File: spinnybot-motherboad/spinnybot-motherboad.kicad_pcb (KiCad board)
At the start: 2 copper layers, 109.4 x 86 mm, 78 parts, among them J1 ENCODER 1, J10 ESC_POS, J11 POWER SW2, J12 LEDSTRIP3, J13 LEDSTRIP2, J14 LEDSTRIP3, J15 BAT_GND, J16 ESC_GND, J2 LEDSTRIP1, J3 LEDSTRIP1, J4 LEDSTRIP2, J5 ENCODER 2, J6 ENCODER 3, J7 SM10B-SRSS-TB, J8 BAT_POS, J9 POWER SW1, Q1 SISA96DN, Q2 SISA96DN, Q3 BC846, Q4 Q_NMOS_DGS, U1 LM1117-3.3, U10 MMA3221KEG, U11 ADS122U04IPWR, U12 ADS122U04IPWR, U2 XBP9B-DMWTB002, U3 MC14504BDR2G, U4 ICM-20649, U5 ESP32-DEVKITC-32D, U6 74LVC1G157GV_125, U7 SN74AHCT541DW, U8 SN74LVC1G18DBVR, U9 MMA3221KEG

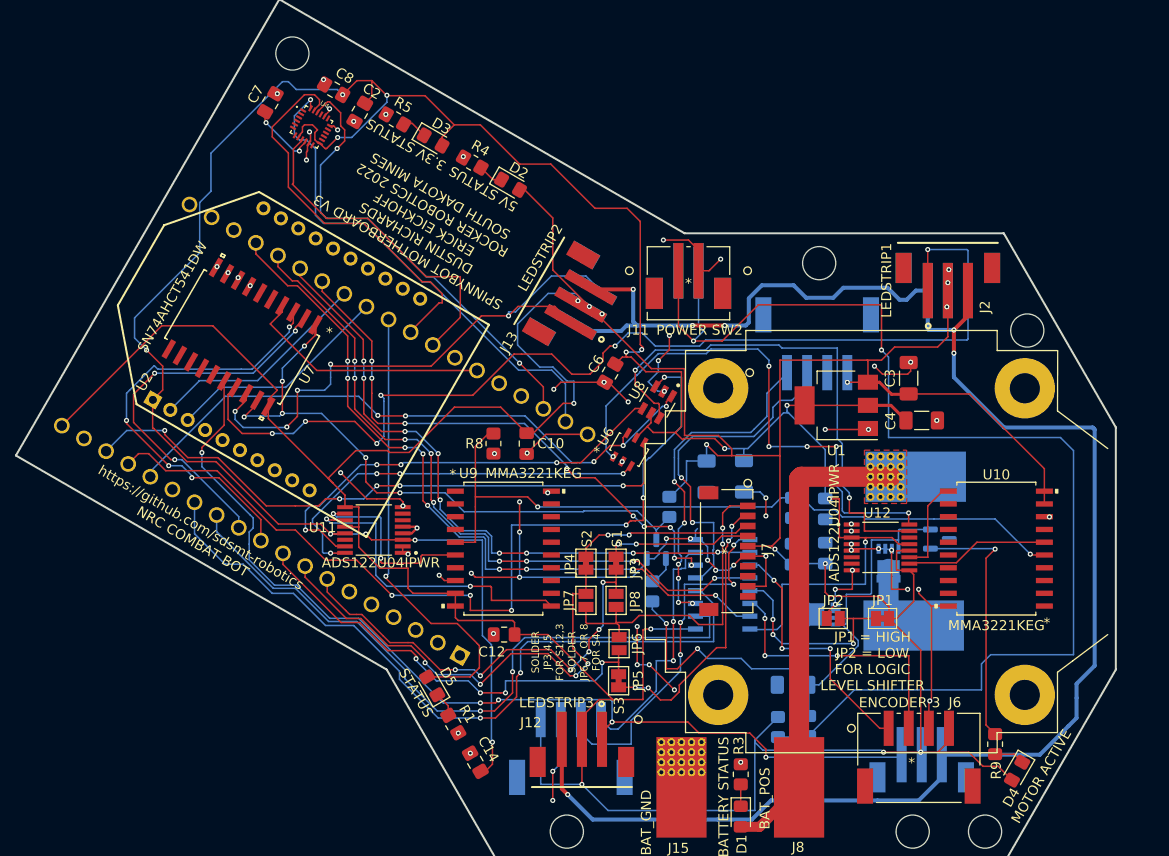
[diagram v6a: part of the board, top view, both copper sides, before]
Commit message: Addressed Pratik's concerns about cap placement and missing caps
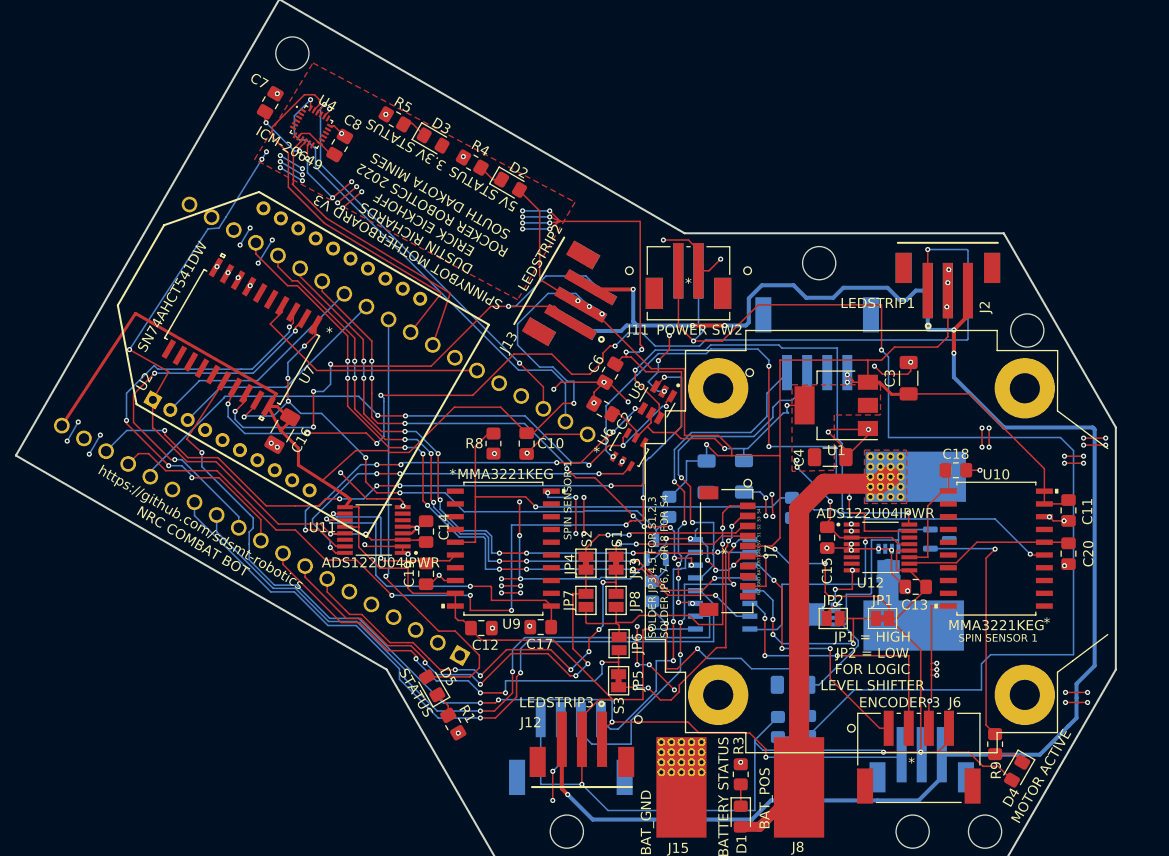
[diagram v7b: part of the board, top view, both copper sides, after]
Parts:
- added C16: 0.1u, Capacitor_SMD:C_1206_3216Metric_Pad1.33x1.80mm_HandSolder, F.Cu at (114.6, 107.1)
- added C17: 10nF, Capacitor_SMD:C_0805_2012Metric_Pad1.18x1.45mm_HandSolder, F.Cu at (140.3, 126.6)
- added C18: 10nF, Capacitor_SMD:C_0805_2012Metric_Pad1.18x1.45mm_HandSolder, F.Cu at (181.6, 111.0)
- added C19: 10nF, Capacitor_SMD:C_0805_2012Metric_Pad1.18x1.45mm_HandSolder, F.Cu at (128.9, 121.3)
- added C20: 10nF, Capacitor_SMD:C_0805_2012Metric_Pad1.18x1.45mm_HandSolder, F.Cu at (192.8, 119.3)
- C11, C13, C15: moved to F.Cu
- moved C2 38.2 mm to (146.5, 104.9), turned to 150 degrees
- moved C11 24.6 mm to (192.8, 115.0), turned to -90 degrees
- moved C14 23.5 mm to (128.9, 117.1), turned to 90 degrees
- moved C13 12.7 mm to (177.6, 122.6), turned to 180 degrees
- moved C4 9.81 mm to (169.1, 109.7)
- moved C8 5.59 mm to (120.3, 78.7), turned to 60 degrees
- moved C15 2.86 mm to (168.8, 117.7)
- moved C12 2.35 mm to (134.4, 126.7), turned to 0 degrees
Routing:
- net +3V3: track 272.1 -> 198.1 mm, vias 14 -> 27
- net GND: track 161.3 -> 235.1 mm, vias 70 -> 116
- net +5V: track 400.5 -> 410.3 mm, vias 15 -> 16
- net /IMU_CS: track 45.8 -> 40.7 mm
- net /MISO_3V3: track 33.3 -> 29.5 mm
- net /MOSI_3V3: track 49.9 -> 47.1 mm
- net Net-(U10-Pad6): track 14.3 -> 16.8 mm
- net Net-(U10-Pad11): track 9.59 -> 11.8 mm
- net Net-(U11-Pad11): track 31.6 -> 33.7 mm
- net +12V: track 47.1 -> 45.3 mm
- net /SCK_3V3: track 39.2 -> 37.7 mm
- net /LEDSTRIP1_DATA_5V: track 106.3 -> 105.1 mm
- net /MCU and Buffers/ENC_1B_3V3: track 74.6 -> 73.7 mm
- net /LEDSTRIP3_DATA_5V: track 98.2 -> 99.1 mm
- net /IMU and Accelerometers/ADC1_RX: track 39.8 -> 39.1 mm
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- added copper zone on F.Cu, net +3V3
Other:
- board text added: "N/C GND BAT CRT GND 5V S1 S2 S3 S4"
- board text added: "SPIN SENSOR 1"

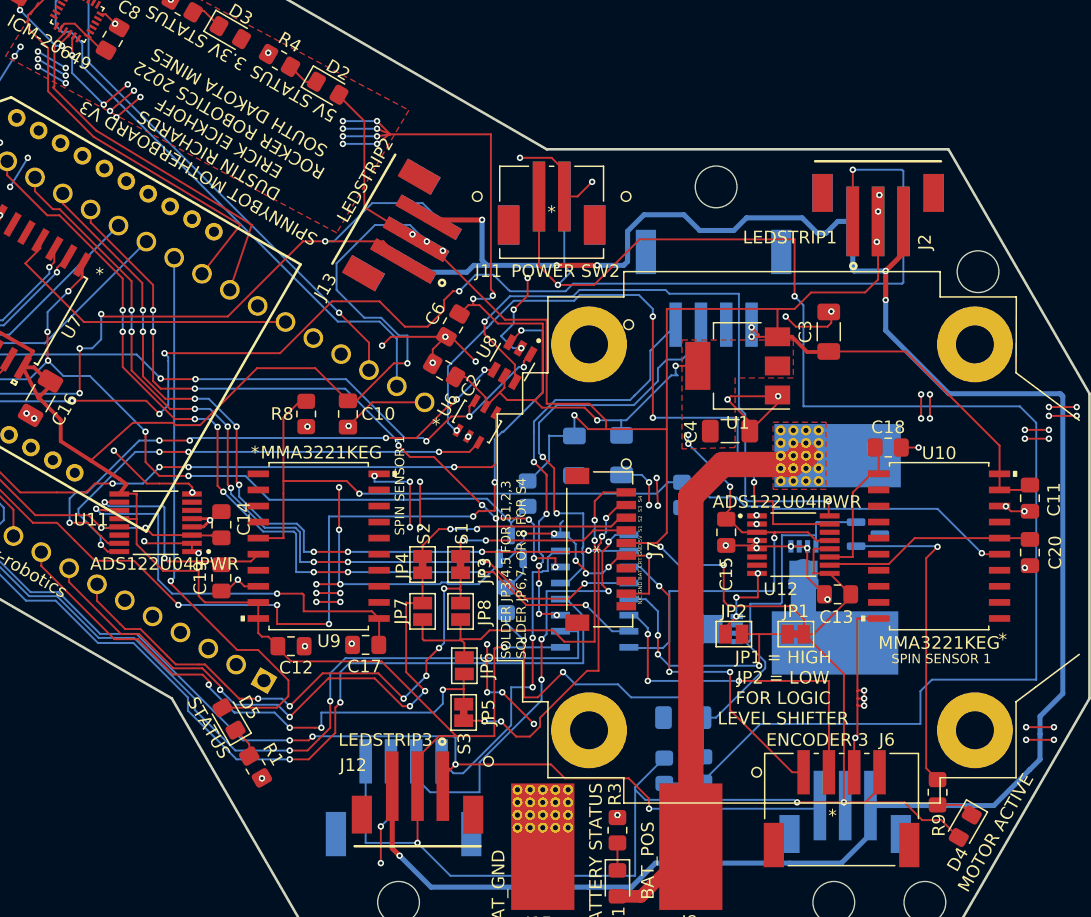
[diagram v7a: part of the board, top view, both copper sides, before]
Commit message: PCB design rule checker fixes, silkscreen overlaps and self-intersecting courtyards
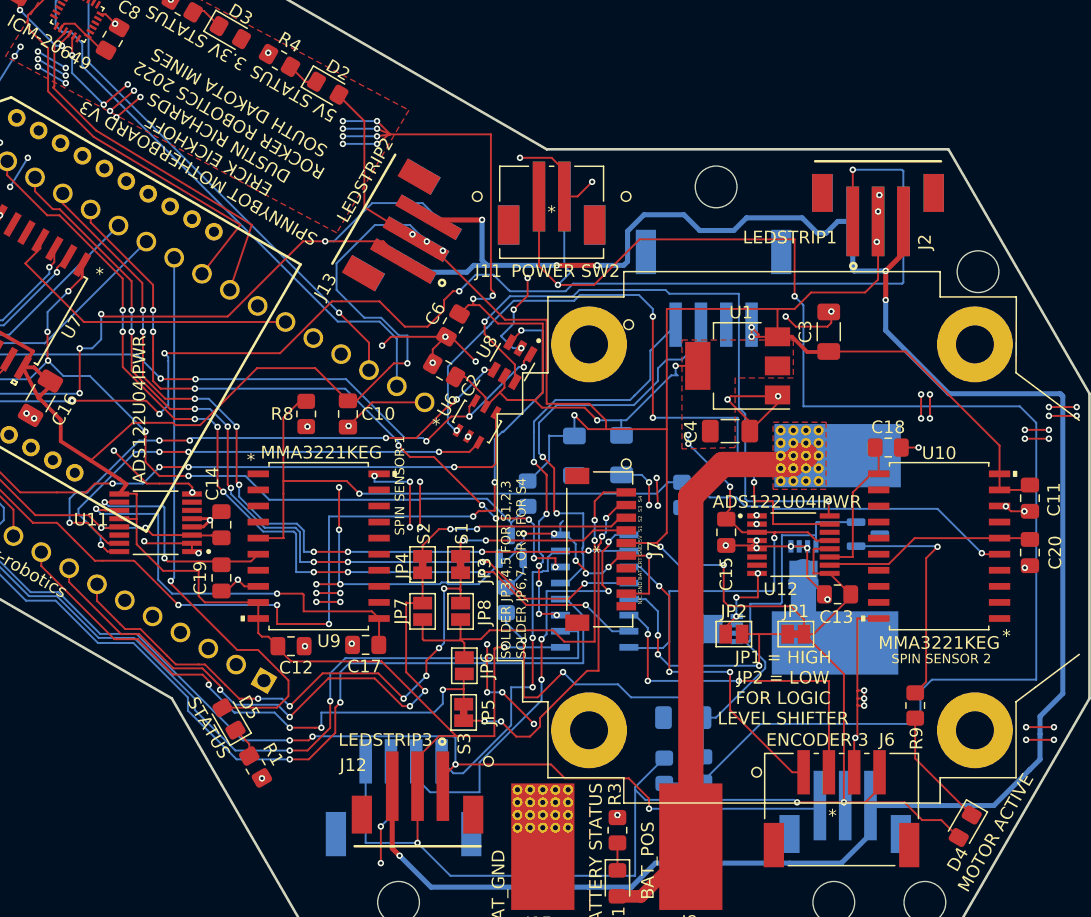
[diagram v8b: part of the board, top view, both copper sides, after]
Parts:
- J7: value SM10B-SRSS-TB -> CONN_SM10B-SRSS-TB_JST
- U6: value 74LVC1G157GV_125 -> TSOP6_SOT457_NEX
- moved R9 7.08 mm to (183.7, 131.3)
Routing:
- net Net-(Q4-Pad1): track 25.6 -> 18.7 mm
- net Net-(D4-Pad1): track 3.03 -> 9.51 mm
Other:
- board text added: "SPIN SENSOR 2"
- board text added: "SPINNYBOT MOTHERBOARD V3 ERICK EICKHOFF DUSTIN RICHARDS ROCKER ROBOTICS 2022 SOUTH DAKOTA MINES"
- board text removed: "SPINNYBOT MOTHERBOARD V3 DUSTIN RICHARDS ERICK EICKHOFF ROCKER ROBOTICS 2022 SOUTH DAKOTA MINES"
